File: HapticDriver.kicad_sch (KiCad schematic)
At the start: 12 parts, among them J14 USB_C_Receptacle_USB2.0, J3 BATT PWR, SW1 BOOT, SW2 EN, U1 ESP32-S3-WROOM-2

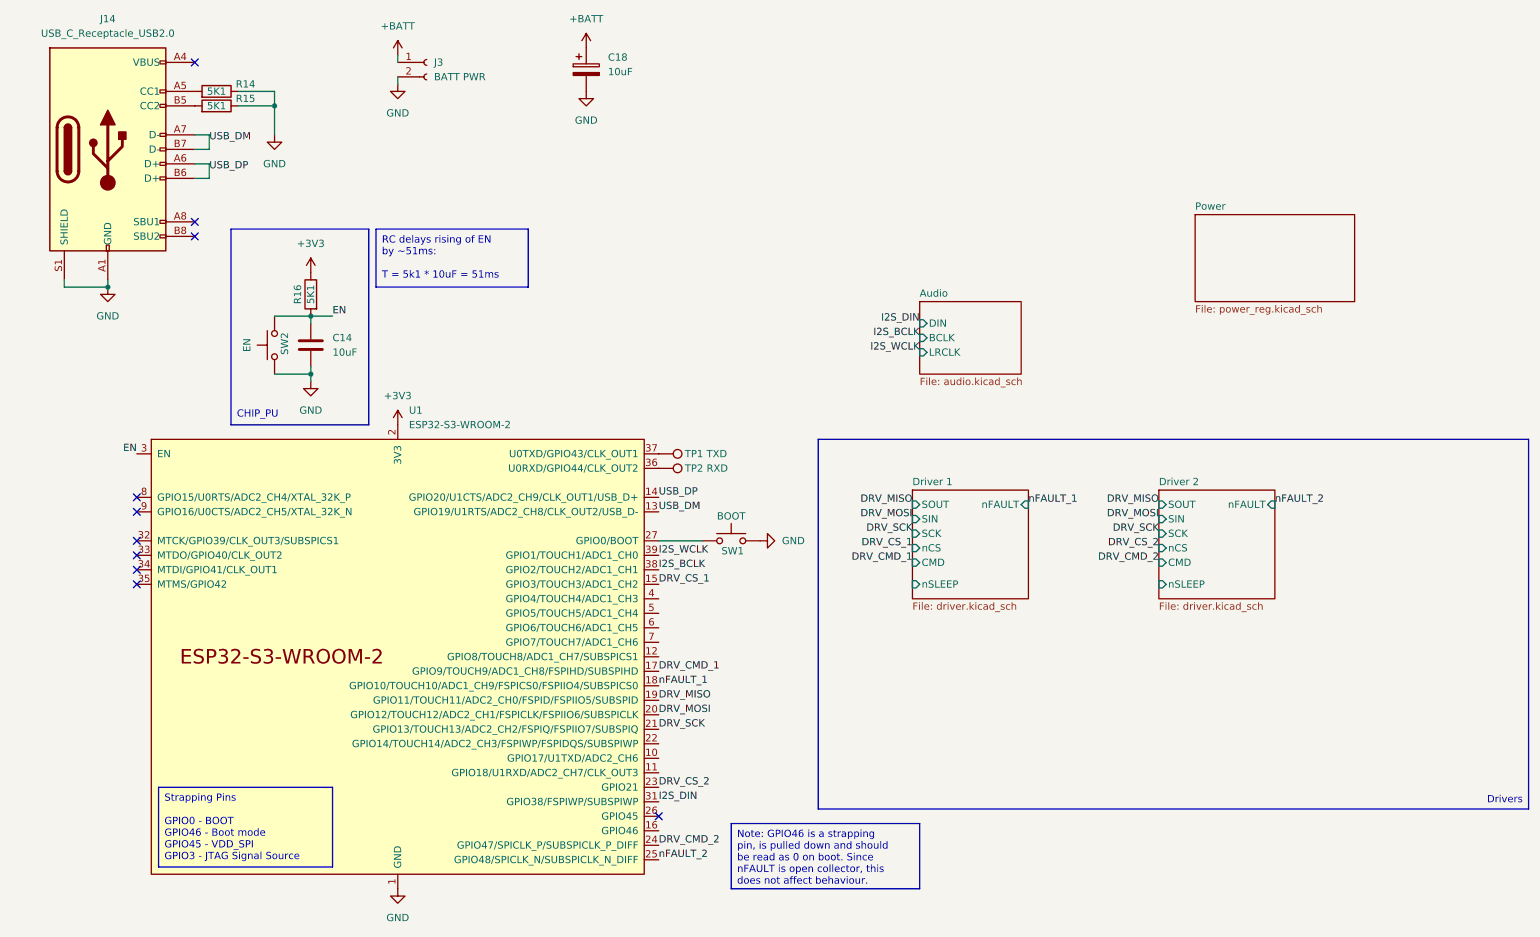
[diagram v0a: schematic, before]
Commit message: feat: fully routed v2 design
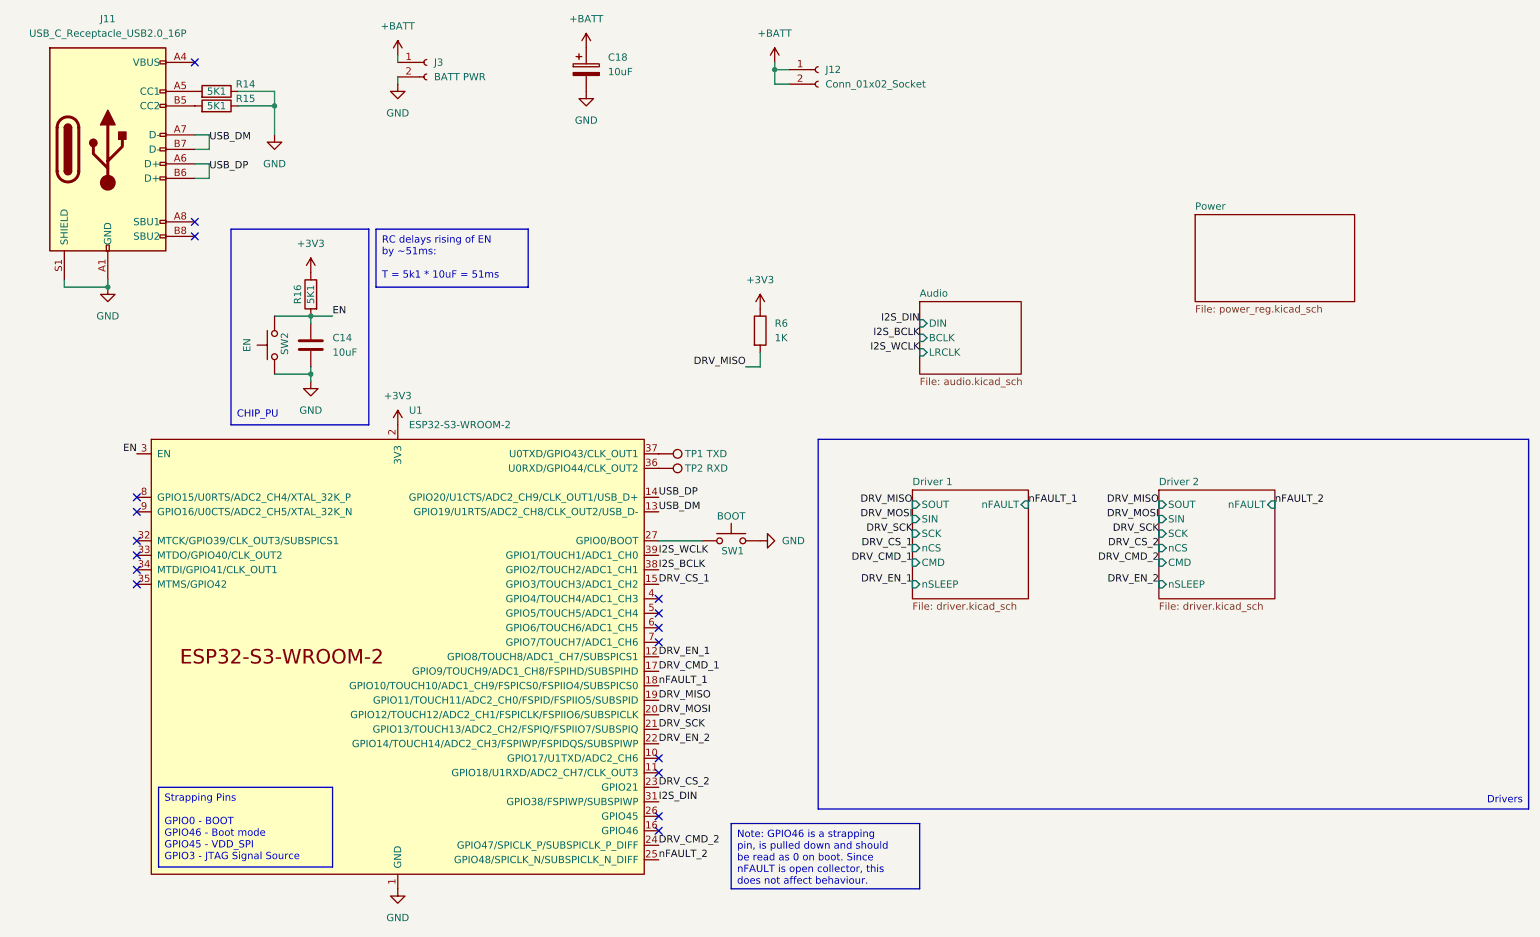
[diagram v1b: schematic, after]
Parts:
- removed J14: USB_C_Receptacle_USB2.0, Connector_USB:USB_C_Receptacle_G-Switch_GT-USB-7010ASV, symbol Connector:USB_C_Receptacle_USB2.0_16P
- added J11: USB_C_Receptacle_USB2.0_16P, Connector_USB:USB_C_Receptacle_G-Switch_GT-USB-7010ASV, symbol Connector:USB_C_Receptacle_USB2.0_16P
- added J12: Conn_01x02_Socket, SolderWires:SolderWire_1x02, symbol Connector:Conn_01x02_Socket
- added R6: 1K, Resistor_SMD:R_0402_1005Metric, symbol Device:R
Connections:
- net +3V3: now also R6.1
- net +BATT: now also J12.1 (Pin_1), J12.2 (Pin_2)
- net DRV_MISO: now also R6.2
- net GND: now also J11.A1 (GND), J11.A12 (GND), J11.B1 (GND), J11.B12 (GND), J11.S1 (SHIELD)
- net USB_DM: now also J11.A7 (D-), J11.B7 (D-)
- net USB_DP: now also J11.A6 (D+), J11.B6 (D+)
- net DRV_EN_1: now reaches U1.12 (GPIO8/TOUCH8/ADC1_CH7/SUBSPICS1)
- net DRV_EN_2: now reaches U1.22 (GPIO14/TOUCH14/ADC2_CH3/FSPIWP/FSPIDQS/SUBSPIWP)
- net at R14.2: now also J11.A5 (CC1)
- net at R15.2: now also J11.B5 (CC2)
- new net: J11.A4 (VBUS), J11.A9 (VBUS), J11.B4 (VBUS), J11.B9 (VBUS)
- no-connect marks 10 -> 17

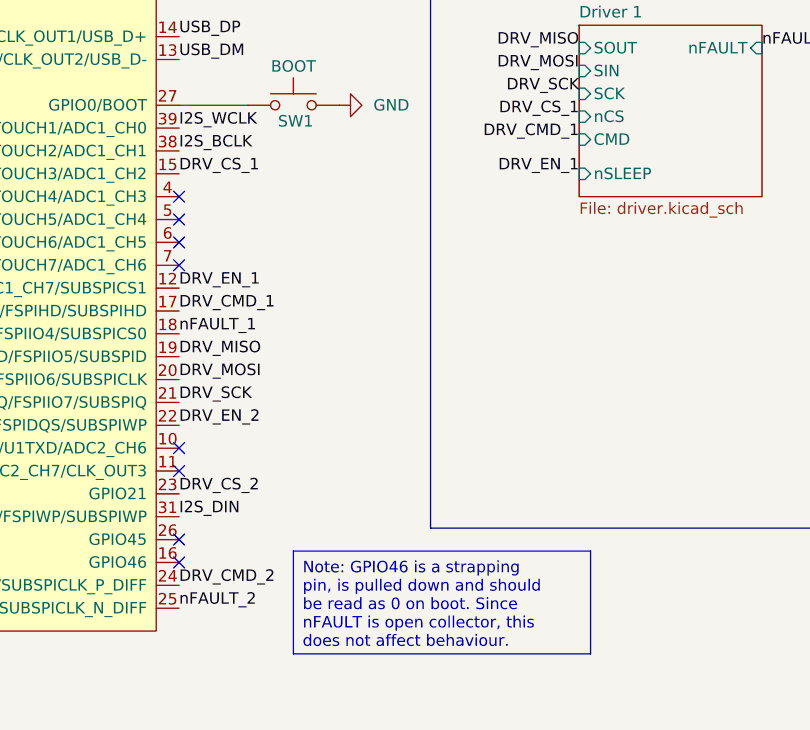
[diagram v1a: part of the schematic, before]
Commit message: feat: battery level measurement resistors
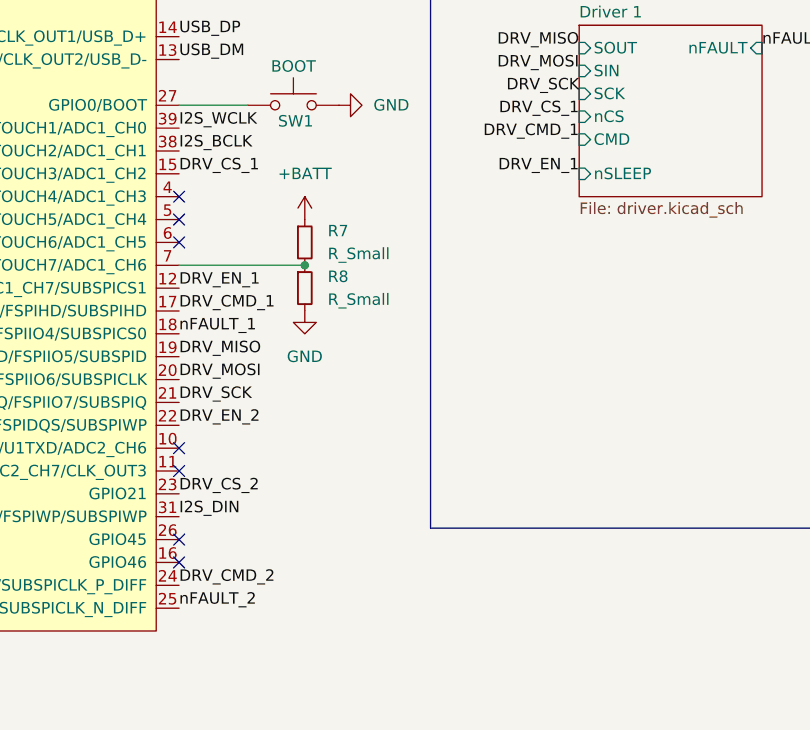
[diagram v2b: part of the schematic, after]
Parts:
- added R7, R8: R_Small, Resistor_SMD:R_0402_1005Metric, symbol Device:R_Small
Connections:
- net +BATT: now also R7.1
- net GND: now also R8.2
- net at U1.7 (GPIO7/TOUCH7/ADC1_CH6): now also R7.2, R8.1
- no-connect marks 17 -> 16

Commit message: feat: populate all jlcpcb part#
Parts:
- C14: Part (none) -> C96446
- J11: Part (none) -> C2988369
- J3: now left out of the parts list
- R14, R15, R16: Part (none) -> C2889415
- R6: Part (none) -> C11702
- R7: value R_Small -> 16K; Part (none) -> C543609
- R8: value R_Small -> 1K; Part (none) -> C11702
- SW1, SW2: footprint Button_Omron:SW_B3U-1000P -> Button_Switch_SMD:SW_Push_1P1T_XKB_TS-1187A; Part (none) -> C318884
- TP1: value TXD -> TX; now left out of the parts list
- TP2: value RXD -> RX; now left out of the parts list
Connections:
- net CODEC_MODE: now reaches U1.32 (MTCK/GPIO39/CLK_OUT3/SUBSPICS1)
- no-connect marks 16 -> 15
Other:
- sheet Audio ports: added MODE; removed none
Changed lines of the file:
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@@
 		(at 128.27 148.59)
 	)
-	(no_connect
-		(at 36.83 110.49)
-	)
 	(wire
 		(pts
@@
 		)
 	)
+	(label "CODEC_MODE"
+		(at 191.77 72.39 0)
+		(fields_autoplaced yes)
+		(effects
+			(font
+				(size 1.27 1.27)
+			)
+			(justify left bottom)
+		)
+	)
 	(label "DRV_MISO"
 		(at 128.27 138.43 0)
@@
 		)
 	)
+	(label "CODEC_MODE"
+		(at 36.83 110.49 180)
+		(fields_autoplaced yes)
+		(effects
+			(font
+				(size 1.27 1.27)
+			)
+			(justify right bottom)
+		)
+	)
 	(label "USB_DM"
 		(at 49.53 40.64 0)
@@
 			)
 		)
-		(property "Value" "R_Small"
+		(property "Value" "1K"
 			(at 144.78 132.0799 0)
 			(effects
@@
 			)
 		)
+		(property "Part" "C11702"
+			(at 142.24 130.81 0)
+			(effects
+				(font
+					(size 1.27 1.27)
+				)
+				(hide yes)
+			)
+		)
 		(pin "1"
 		)
@@
 			)
 		)
+		(property "Part" "C2889415"
+			(at 67.31 67.31 90)
+			(effects
+				(font
+					(size 1.27 1.27)
+				)
+				(hide yes)
+			)
+		)
 		(pin "1"
 		)
@@
 		(unit 1)
 		(exclude_from_sim no)
-		(in_bom yes)
+		(in_bom no)
 		(on_board yes)
 		(dnp no)
@@
 			)
 		)
+		(property "Part" "C11702"
+			(at 146.05 73.66 0)
+			(effects
+				(font
+					(size 1.27 1.27)
+				)
+				(hide yes)
+			)
+		)
 		(pin "2"
 		)
@@
 		(on_board yes)
 		(dnp no)
-		(fields_autoplaced yes)
 		(property "Reference" "#PWR036"
 			(at 142.24 127 0)
@@
 		)
 		(property "Value" "+BATT"
-			(at 142.24 118.11 0)
+			(at 142.24 118.872 0)
 			(effects
 				(font
@@
 			)
 		)
-		(property "Footprint" "Button_Omron:SW_B3U-1000P"
+		(property "Footprint" "Button_Switch_SMD:SW_Push_1P1T_XKB_TS-1187A"
 			(at 140.97 105.41 0)
 			(effects
@@
 			)
 		)
-		(property "Datasheet" "https://omronfs.omron.com/en_US/ecb/products/pdf/en-b3fs.pdf"
+		(property "Datasheet" ""
 			(at 140.97 105.41 0)
 			(effects
@@
 			)
 		)
-		(property "Description" "Omron B3FS 6x6mm single pole normally-open tactile switch"
+		(property "Description" ""
+			(at 140.97 110.49 0)
+			(effects
+				(font
+					(size 1.27 1.27)
+				)
+				(hide yes)
+			)
+		)
+		(property "Part" "C318884"
 			(at 140.97 110.49 0)
 			(effects
@@
 		(unit 1)
 		(exclude_from_sim no)
-		(in_bom yes)
+		(in_bom no)
 		(on_board yes)
 		(dnp no)
@@
 			)
 		)
-		(property "Value" "RXD"
+		(property "Value" "RX"
 			(at 136.652 97.79 90)
 			(effects
@@
 			)
 		)
-		(property "Footprint" "Button_Omron:SW_B3U-1000P"
+		(property "Footprint" "Button_Switch_SMD:SW_Push_1P1T_XKB_TS-1187A"
 			(at 55.88 76.2 0)
 			(effects
@@
 			)
 		)
-		(property "Datasheet" "https://omronfs.omron.com/en_US/ecb/products/pdf/en-b3fs.pdf"
+		(property "Datasheet" ""
 			(at 55.88 76.2 0)
 			(effects
@@
 			)
 		)
-		(property "Description" "Omron B3FS 6x6mm single pole normally-open tactile switch"
+		(property "Description" ""
+			(at 60.96 76.2 0)
+			(effects
+				(font
+					(size 1.27 1.27)
+				)
+				(hide yes)
+			)
+		)
+		(property "Part" "C318884"
 			(at 60.96 76.2 0)
 			(effects
@@
 			)
 		)
+		(property "Part" "C2889415"
+			(at 50.8 34.29 90)
+			(effects
+				(font
+					(size 1.27 1.27)
+				)
+				(hide yes)
+			)
+		)
 		(pin "1"
 		)
@@
 			)
 		)
+		(property "Part" "C96446"
+			(at 67.31 76.2 0)
+			(effects
+				(font
+					(size 1.27 1.27)
+				)
+				(hide yes)
+			)
+		)
 		(pin "2"
 		)
@@
 			)
 		)
-		(property "Value" "R_Small"
+		(property "Value" "16K"
 			(at 144.78 126.9999 0)
 			(effects
@@
 			)
 		)
+		(property "Part" "C543609"
+			(at 142.24 125.73 0)
+			(effects
+				(font
+					(size 1.27 1.27)
+				)
+				(hide yes)
+			)
+		)
 		(pin "1"
 		)
@@
 			)
 		)
+		(property "Part" "C2988369"
+			(at 31.75 41.91 0)
+			(effects
+				(font
+					(size 1.27 1.27)
+				)
+				(hide yes)
+			)
+		)
 		(pin "B6"
 		)
@@
 			)
 		)
+		(property "Part" "C2889415"
+			(at 50.8 31.75 90)
+			(effects
+				(font
+					(size 1.27 1.27)
+				)
+				(hide yes)
+			)
+		)
 		(pin "1"
 		)
@@
 		(unit 1)
 		(exclude_from_sim no)
-		(in_bom yes)
+		(in_bom no)
 		(on_board yes)
 		(dnp no)
@@
 			)
 		)
-		(property "Value" "TXD"
+		(property "Value" "TX"
 			(at 136.652 95.25 90)
 			(effects
@@
 			)
 		)
+		(pin "MODE" input
+			(at 191.77 72.39 0)
+			(effects
+				(font
+					(size 1.27 1.27)
+				)
+				(justify right)
+			)
+		)
